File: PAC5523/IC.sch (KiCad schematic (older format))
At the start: 17 parts

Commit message: updated schematic
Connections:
- net 3V3 is gone; now on net +5V: U?.8 (VCC)
- net VIO is gone; now on net +5V: U?.16 (VCC), U?.5 (VBUS), U?.5 (VBUS), U?.5 (VBUS)
- net VSYS is gone; now on net +5V: U?.3 (VDD)
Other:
- moved on the sheet: C?, D?, L?, R?, U?

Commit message: updated schematic
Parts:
- C?: value 10uF -> 100n; footprint Capacitor_SMD:C_0805_2012Metric -> Capacitor_SMD:C_0603_1608Metric
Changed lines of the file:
@@
 P 2550 1300
 F 0 "C?" H 2642 1346 50  0000 L CNN
-F 1 "10uF" H 2642 1255 50  0000 L CNN
-F 2 "Capacitor_SMD:C_0805_2012Metric" H 2550 1300 50  0001 C CNN
+F 1 "100n" H 2642 1255 50  0000 L CNN
+F 2 "Capacitor_SMD:C_0603_1608Metric" H 2550 1300 50  0001 C CNN
 F 3 "~" H 2550 1300 50  0001 C CNN
 	1    2550 1300

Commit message: wip
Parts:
- U4: renamed from U?; footprint Package_SO:SOIC-16W_5.3x10.2mm_P1.27mm -> Package_SO:SOIC-16_3.9x9.9mm_P1.27mm
- U5: renamed from U?; footprint (none) -> Package_TO_SOT_SMD:SOT-23-5
- gave numbers to parts that had none: 15
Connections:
- net ENC_B: no longer U3.4 (RXD)
- net RS485RXTX: no longer U3.1 (TXD)
- new net CANRX: U3.4 (RXD)
- new net CANTX: U3.1 (TXD)

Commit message: wip
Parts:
- D17: footprint Diode_SMD:D_SMA -> Diode_SMD:D_SOD-123F
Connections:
- net Ain: now also U9.6 (IO4); no longer U7.6 (IO4)
- net CANRX: now also U6.1 (DI), U9.1 (IO1)
- net CANTX: now also U6.4 (DO), U9.3 (IO2)
- net HALL1: now also U8.4 (IO3); no longer U8.6 (IO4)
- net HALL2: now also U8.6 (IO4); no longer U8.4 (IO3)
- net NTC: now also U7.1 (IO1); no longer U7.4 (IO3)
- net SWDCL: now also U7.6 (IO4); no longer U9.6 (IO4)
- net SWDIO: now also U7.4 (IO3); no longer U9.4 (IO3)
- removed net UART_RX: U6.4 (DO), U9.1 (IO1)
- removed net UART_TX: U6.1 (DI), U9.3 (IO2)
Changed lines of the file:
@@
 F 0 "D17" H 2550 2005 50  0000 C CNN
 F 1 "SS310" H 2550 1914 50  0000 C CNN
-F 2 "Diode_SMD:D_SMA" V 2550 1800 50  0001 C CNN
+F 2 "Diode_SMD:D_SOD-123F" V 2550 1800 50  0001 C CNN
 F 3 "~" V 2550 1800 50  0001 C CNN
 	1    2550 1800
@@
 Wire Wire Line
 	6200 4550 6200 4650
-Text GLabel 6200 4750 0    50   Input ~ 0
-UART_RX
-Text GLabel 6200 4450 0    50   Input ~ 0
-UART_TX
 $Comp
 L otter:RS485 U6
@@
 	1    0    0    -1
 $EndComp
+Text GLabel 9550 3350 2    50   Input ~ 0
+SWDCL
+Text GLabel 9550 3450 2    50   Input ~ 0
+SWDIO
+Text GLabel 8950 3250 0    50   Input ~ 0
+NTC
 Text GLabel 9550 4550 2    50   Input ~ 0
-SWDCL
-Text GLabel 9550 4650 2    50   Input ~ 0
-SWDIO
-Text GLabel 9550 3450 2    50   Input ~ 0
-NTC
-Text GLabel 9550 3350 2    50   Input ~ 0
 Ain
 $Comp
@@
 	1    0    0    -1
 $EndComp
-Text GLabel 8950 4450 0    50   Input ~ 0
-UART_RX
-Text GLabel 8950 4550 0    50   Input ~ 0
-UART_TX
 $Comp
 L power:GND #PWR0166
@@
 Text GLabel 8950 3850 0    50   Input ~ 0
 HALL3
+Text GLabel 9550 3950 2    50   Input ~ 0
+HALL2
 Text GLabel 9550 4050 2    50   Input ~ 0
-HALL2
-Text GLabel 9550 3950 2    50   Input ~ 0
 HALL1
 $Comp
@@
 Text GLabel 2350 3600 0    50   Input ~ 0
 CANTX
+Text GLabel 8950 4450 0    50   Input ~ 0
+CANRX
+Text GLabel 8950 4550 0    50   Input ~ 0
+CANTX
+Text GLabel 6200 4750 0    50   Input ~ 0
+CANTX
+Text GLabel 6200 4450 0    50   Input ~ 0
+CANRX
 $EndSCHEMATC

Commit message: wip
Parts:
- U5: footprint Package_TO_SOT_SMD:SOT-23-5 -> Package_TO_SOT_SMD:SOT-353_SC-70-5
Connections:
- net NTC: now also U7.4 (IO3); no longer U7.1 (IO1)
- net SWDCL: now also U7.3 (IO2); no longer U7.6 (IO4)
- net SWDIO: now also U7.1 (IO1); no longer U7.4 (IO3)
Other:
- note removed: "Braucht Footprint ^"
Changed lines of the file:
@@
 	1    0    0    -1
 $EndComp
-Text Notes 5950 3700 0    50   ~ 0
-Braucht Footprint ^
 Text GLabel 6850 3300 2    50   Input ~ 0
 SK6812_OUT
@@
 F 0 "U5" H 6525 3525 50  0000 C CNN
 F 1 "NL17SZ125" H 6525 3434 50  0000 C CNN
-F 2 "Package_TO_SOT_SMD:SOT-23-5" H 6500 3400 50  0001 C CNN
+F 2 "Package_TO_SOT_SMD:SOT-353_SC-70-5" H 6500 3400 50  0001 C CNN
 F 3 "https://lcsc.com/product-detail/Logic-ICs_ON-Semicon_NL17SZ125DFT2G_ON-Semicon-ON-NL17SZ125DFT2G_C97774.html" H 6500 3400 50  0001 C CNN
 	1    6500 3200
@@
 	1    0    0    -1
 $EndComp
-Text GLabel 9550 3350 2    50   Input ~ 0
+Text GLabel 8950 3350 0    50   Input ~ 0
 SWDCL
+Text GLabel 8950 3250 0    50   Input ~ 0
+SWDIO
 Text GLabel 9550 3450 2    50   Input ~ 0
-SWDIO
-Text GLabel 8950 3250 0    50   Input ~ 0
 NTC
 Text GLabel 9550 4550 2    50   Input ~ 0

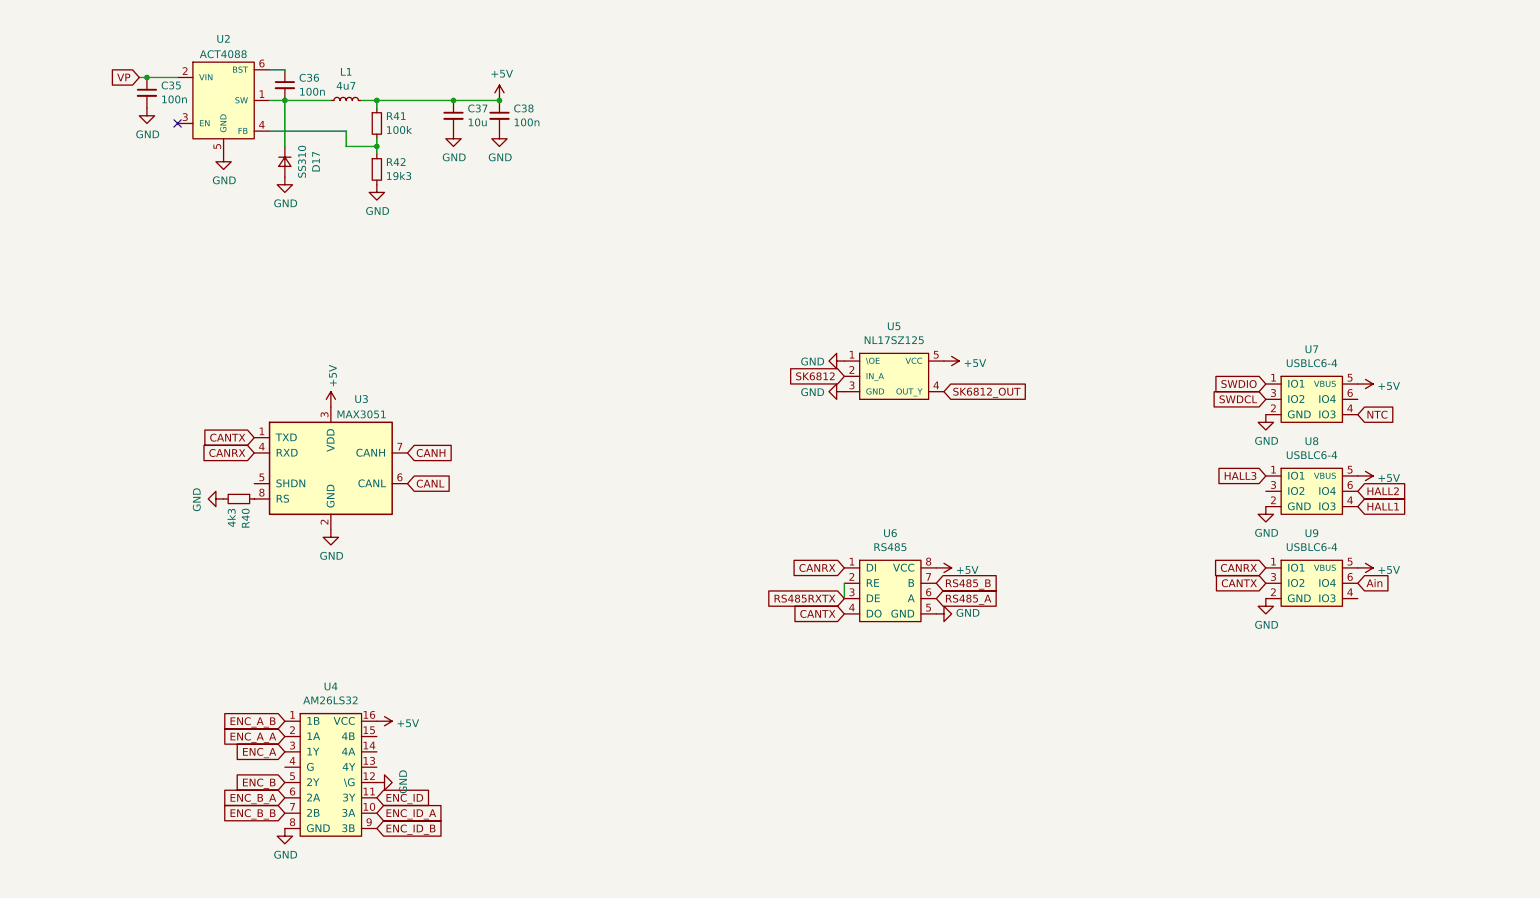
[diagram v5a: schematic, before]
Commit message: added Encoder,LED,NTC
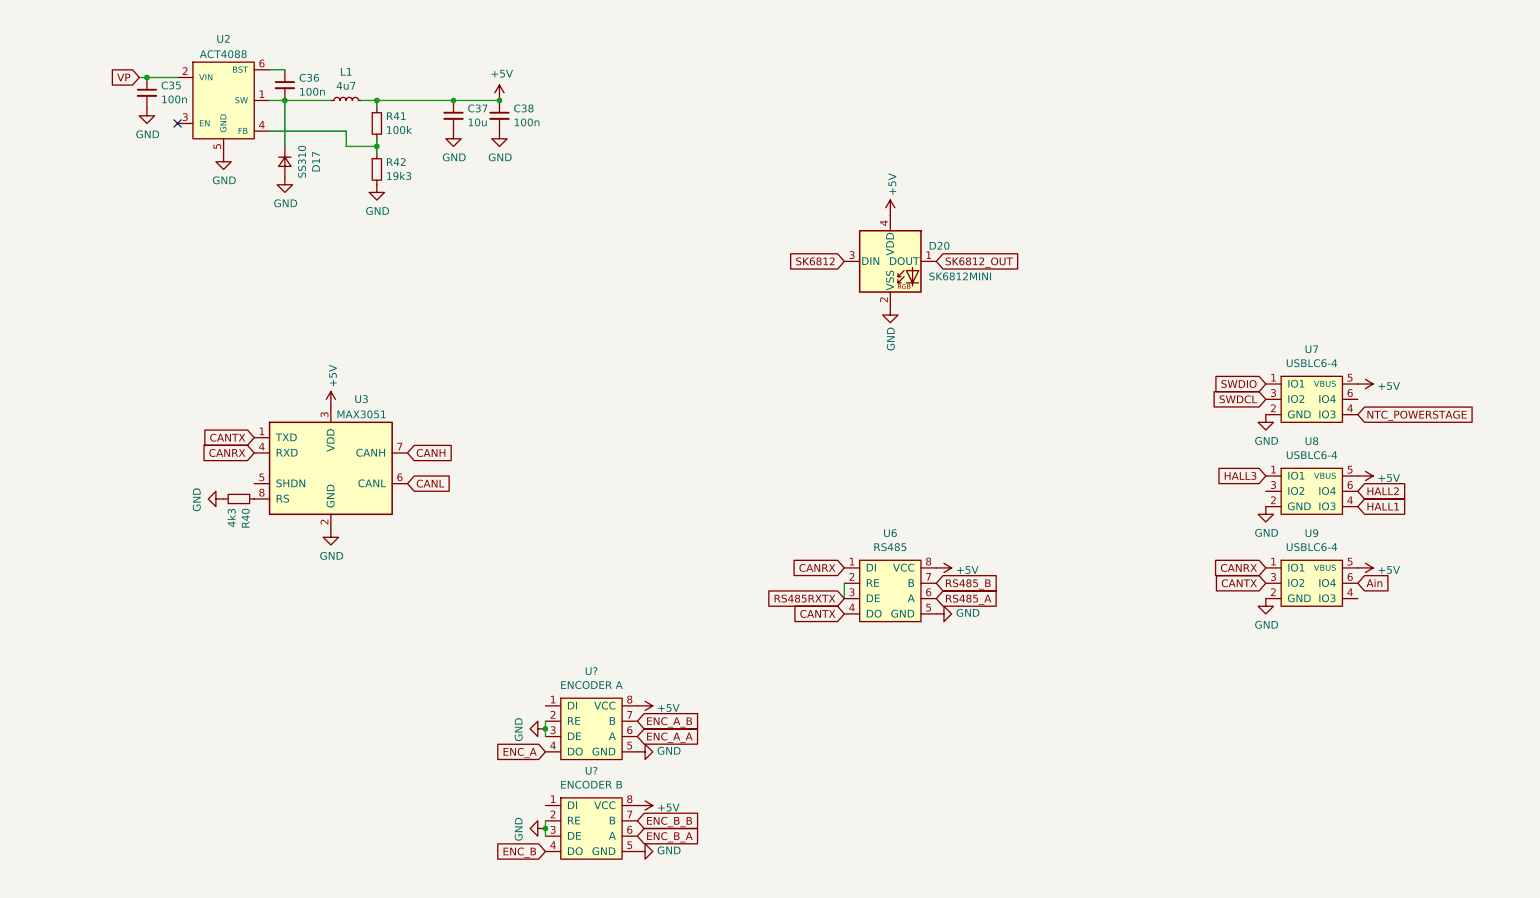
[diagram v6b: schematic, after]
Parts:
- removed U4: AM26LS32, Package_SO:SOIC-16_3.9x9.9mm_P1.27mm, symbol otter:AM26LS32
- removed U5: NL17SZ125, Package_TO_SOT_SMD:SOT-353_SC-70-5, symbol otter:NL17SZ125
- added D20: SK6812MINI, LED_SMD:LED_SK6812MINI_PLCC4_3.5x3.5mm_P1.75mm, symbol LED:SK6812MINI
- added U?: ENCODER A, Package_SO:SOIC-8_3.9x4.9mm_P1.27mm, symbol otter:RS485
- added U?: ENCODER B, Package_SO:SOIC-8_3.9x4.9mm_P1.27mm, symbol otter:RS485
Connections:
- net +5V: now also D20.4 (VDD), U?.8 (VCC), U?.8 (VCC)
- net ENC_A: now also U?.4 (DO)
- net ENC_A_A: now also U?.6 (A)
- net ENC_A_B: now also U?.7 (B)
- net ENC_B: now also U?.4 (DO)
- net ENC_B_A: now also U?.6 (A)
- net ENC_B_B: now also U?.7 (B)
- net GND: now also D20.2 (VSS), U?.2 (RE), U?.2 (RE), U?.3 (DE), U?.3 (DE), U?.5 (GND), U?.5 (GND)
- net SK6812: now also D20.3 (DIN)
- net SK6812_OUT: now also D20.1 (DOUT)
- net NTC renamed NTC_POWERSTAGE
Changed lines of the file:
@@
 L power:+5V #PWR0150
 U 1 1 5D5D3803
-P 6850 3100
-F 0 "#PWR0150" H 6850 2950 50  0001 C CNN
-F 1 "+5V" V 6865 3228 50  0000 L CNN
-F 2 "" H 6850 3100 50  0001 C CNN
-F 3 "" H 6850 3100 50  0001 C CNN
-	1    6850 3100
-	0    1    1    0
+P 6500 2150
+F 0 "#PWR0150" H 6500 2000 50  0001 C CNN
+F 1 "+5V" V 6515 2278 50  0000 L CNN
+F 2 "" H 6500 2150 50  0001 C CNN
+F 3 "" H 6500 2150 50  0001 C CNN
+	1    6500 2150
+	1    0    0    -1
 $EndComp
 Connection ~ 3950 1400
@@
 	1    0    0    -1
 $EndComp
-Text GLabel 6850 3300 2    50   Input ~ 0
+Text GLabel 6800 2450 2    50   Input ~ 0
 SK6812_OUT
-Text GLabel 6200 3200 0    50   Input ~ 0
+Text GLabel 6200 2450 0    50   Input ~ 0
 SK6812
-$Comp
-L power:GND #PWR0158
-U 1 1 5D5D3883
-P 6200 3100
-F 0 "#PWR0158" H 6200 2850 50  0001 C CNN
-F 1 "GND" V 6205 2972 50  0000 R CNN
-F 2 "" H 6200 3100 50  0001 C CNN
-F 3 "" H 6200 3100 50  0001 C CNN
-	1    6200 3100
-	0    1    1    0
-$EndComp
 $Comp
 L power:GND #PWR0159
 U 1 1 5D5D3889
-P 6200 3300
-F 0 "#PWR0159" H 6200 3050 50  0001 C CNN
-F 1 "GND" V 6205 3172 50  0000 R CNN
-F 2 "" H 6200 3300 50  0001 C CNN
-F 3 "" H 6200 3300 50  0001 C CNN
-	1    6200 3300
-	0    1    1    0
-$EndComp
-$Comp
-L otter:NL17SZ125 U5
-U 1 1 5D5D388F
-P 6500 3200
-F 0 "U5" H 6525 3525 50  0000 C CNN
-F 1 "NL17SZ125" H 6525 3434 50  0000 C CNN
-F 2 "Package_TO_SOT_SMD:SOT-353_SC-70-5" H 6500 3400 50  0001 C CNN
-F 3 "https://lcsc.com/product-detail/Logic-ICs_ON-Semicon_NL17SZ125DFT2G_ON-Semicon-ON-NL17SZ125DFT2G_C97774.html" H 6500 3400 50  0001 C CNN
-	1    6500 3200
+P 6500 2750
+F 0 "#PWR0159" H 6500 2500 50  0001 C CNN
+F 1 "GND" V 6505 2622 50  0000 R CNN
+F 2 "" H 6500 2750 50  0001 C CNN
+F 3 "" H 6500 2750 50  0001 C CNN
+	1    6500 2750
 	1    0    0    -1
 $EndComp
@@
 	1    0    0    -1
 $EndComp
-$Comp
-L power:GND #PWR0162
-U 1 1 5D5D38C4
-P 3150 5850
-F 0 "#PWR0162" H 3150 5600 50  0001 C CNN
-F 1 "GND" H 3155 5677 50  0000 C CNN
-F 2 "" H 3150 5850 50  0001 C CNN
-F 3 "" H 3150 5850 50  0001 C CNN
-	1    3150 5850
-	0    -1   -1   0
-$EndComp
-Text GLabel 3150 6150 2    50   Input ~ 0
-ENC_ID_B
-Text GLabel 3150 6050 2    50   Input ~ 0
-ENC_ID_A
-Text GLabel 2550 6050 0    50   Input ~ 0
+Text GLabel 4850 6100 2    50   Input ~ 0
 ENC_B_B
-Text GLabel 2550 5950 0    50   Input ~ 0
+Text GLabel 4850 6200 2    50   Input ~ 0
 ENC_B_A
-Text GLabel 2550 5550 0    50   Input ~ 0
+Text GLabel 4850 5550 2    50   Input ~ 0
 ENC_A_A
-Text GLabel 2550 5450 0    50   Input ~ 0
+Text GLabel 4850 5450 2    50   Input ~ 0
 ENC_A_B
-$Comp
-L power:GND #PWR0163
-U 1 1 5D5D38D1
-P 2550 6150
-F 0 "#PWR0163" H 2550 5900 50  0001 C CNN
-F 1 "GND" H 2555 5977 50  0000 C CNN
-F 2 "" H 2550 6150 50  0001 C CNN
-F 3 "" H 2550 6150 50  0001 C CNN
-	1    2550 6150
-	1    0    0    -1
-$EndComp
-$Comp
-L otter:AM26LS32 U4
-U 1 1 5D5D38D7
-P 2850 5800
-F 0 "U4" H 2850 6375 50  0000 C CNN
-F 1 "AM26LS32" H 2850 6284 50  0000 C CNN
-F 2 "Package_SO:SOIC-16_3.9x9.9mm_P1.27mm" H 2850 6350 50  0001 C CNN
-F 3 "https://lcsc.com/product-detail/Driver-ICs_TI_AM26C32IDR_AM26C32IDR_C36693.html" H 2850 6350 50  0001 C CNN
-	1    2850 5800
-	1    0    0    -1
-$EndComp
-Text GLabel 2550 5850 0    50   Input ~ 0
+Text GLabel 4250 6300 0    50   Input ~ 0
 ENC_B
-Text GLabel 2550 5650 0    50   Input ~ 0
+Text GLabel 4250 5650 0    50   Input ~ 0
 ENC_A
-Text GLabel 3150 5950 2    50   Input ~ 0
-ENC_ID
 $Comp
 L power:GND #PWR0164
@@
 SWDIO
 Text GLabel 9550 3450 2    50   Input ~ 0
-NTC
+NTC_POWERSTAGE
 Text GLabel 9550 4550 2    50   Input ~ 0
 Ain
@@
 Text GLabel 9550 4050 2    50   Input ~ 0
 HALL1
-$Comp
-L power:+5V #PWR0168
-U 1 1 5D6006D6
-P 3150 5450
-F 0 "#PWR0168" H 3150 5300 50  0001 C CNN
-F 1 "+5V" V 3165 5578 50  0000 L CNN
-F 2 "" H 3150 5450 50  0001 C CNN
-F 3 "" H 3150 5450 50  0001 C CNN
-	1    3150 5450
-	0    1    1    0
-$EndComp
 $Comp
 L power:+5V #PWR0169
@@
 Text GLabel 6200 4450 0    50   Input ~ 0
 CANRX
+$Comp
+L LED:SK6812MINI D20
+U 1 1 5CDB4E22
+P 6500 2450
+F 0 "D20" H 6750 2550 50  0000 L CNN
+F 1 "SK6812MINI" H 6750 2350 50  0000 L CNN
+F 2 "LED_SMD:LED_SK6812MINI_PLCC4_3.5x3.5mm_P1.75mm" H 6550 2150 50  0001 L TNN
+F 3 "https://cdn-shop.adafruit.com/product-files/2686/SK6812MINI_REV.01-1-2.pdf" H 6600 2075 50  0001 L TNN
+	1    6500 2450
+	1    0    0    -1
+$EndComp
+$Comp
+L power:GND #PWR?
+U 1 1 5CDFFD7B
+P 4850 5650
+F 0 "#PWR?" H 4850 5400 50  0001 C CNN
+F 1 "GND" V 4855 5522 50  0000 R CNN
+F 2 "" H 4850 5650 50  0001 C CNN
+F 3 "" H 4850 5650 50  0001 C CNN
+	1    4850 5650
+	0    -1   -1   0
+$EndComp
+Wire Wire Line
+	4250 5450 4250 5500
+$Comp
+L otter:RS485 U?
+U 1 1 5CDFFD85
+P 4550 5500
+F 0 "U?" H 4550 5875 50  0000 C CNN
+F 1 "ENCODER A" H 4550 5784 50  0000 C CNN
+F 2 "Package_SO:SOIC-8_3.9x4.9mm_P1.27mm" H 4550 5750 50  0001 C CNN
+F 3 "" H 4550 5750 50  0001 C CNN
+	1    4550 5500
+	1    0    0    -1
+$EndComp
+$Comp
+L power:+5V #PWR?
+U 1 1 5CDFFD8B
+P 4850 5350
+F 0 "#PWR?" H 4850 5200 50  0001 C CNN
+F 1 "+5V" V 4865 5478 50  0000 L CNN
+F 2 "" H 4850 5350 50  0001 C CNN
+F 3 "" H 4850 5350 50  0001 C CNN
+	1    4850 5350
+	0    1    1    0
+$EndComp
+$Comp
+L power:GND #PWR?
+U 1 1 5CE00508
+P 4850 6300
+F 0 "#PWR?" H 4850 6050 50  0001 C CNN
+F 1 "GND" V 4855 6172 50  0000 R CNN
+F 2 "" H 4850 6300 50  0001 C CNN
+F 3 "" H 4850 6300 50  0001 C CNN
+	1    4850 6300
+	0    -1   -1   0
+$EndComp
+Wire Wire Line
+	4250 6100 4250 6150
+$Comp
+L otter:RS485 U?
+U 1 1 5CE00512
+P 4550 6150
+F 0 "U?" H 4550 6525 50  0000 C CNN
+F 1 "ENCODER B" H 4550 6434 50  0000 C CNN
+F 2 "Package_SO:SOIC-8_3.9x4.9mm_P1.27mm" H 4550 6400 50  0001 C CNN
+F 3 "" H 4550 6400 50  0001 C CNN
+	1    4550 6150
+	1    0    0    -1
+$EndComp
+$Comp
+L power:+5V #PWR?
+U 1 1 5CE00518
+P 4850 6000
+F 0 "#PWR?" H 4850 5850 50  0001 C CNN
+F 1 "+5V" V 4865 6128 50  0000 L CNN
+F 2 "" H 4850 6000 50  0001 C CNN
+F 3 "" H 4850 6000 50  0001 C CNN
+	1    4850 6000
+	0    1    1    0
+$EndComp
+$Comp
+L power:GND #PWR?
+U 1 1 5CE03BAB
+P 4250 6150
+F 0 "#PWR?" H 4250 5900 50  0001 C CNN
+F 1 "GND" H 4255 5977 50  0000 C CNN
+F 2 "" H 4250 6150 50  0001 C CNN
+F 3 "" H 4250 6150 50  0001 C CNN
+	1    4250 6150
+	0    1    1    0
+$EndComp
+$Comp
+L power:GND #PWR?
+U 1 1 5CE03EB0
+P 4250 5500
+F 0 "#PWR?" H 4250 5250 50  0001 C CNN
+F 1 "GND" H 4255 5327 50  0000 C CNN
+F 2 "" H 4250 5500 50  0001 C CNN
+F 3 "" H 4250 5500 50  0001 C CNN
+	1    4250 5500
+	0    1    1    0
+$EndComp
+Connection ~ 4250 5500
+Wire Wire Line
+	4250 5500 4250 5550
+Connection ~ 4250 6150
+Wire Wire Line
+	4250 6150 4250 6200
 $EndSCHEMATC

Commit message: wip
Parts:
- gave numbers to parts that had none: 2
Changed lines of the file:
@@
 $EndComp
 $Comp
-L power:GND #PWR?
+L power:GND #PWR0168
 U 1 1 5CDFFD7B
 P 4850 5650
-F 0 "#PWR?" H 4850 5400 50  0001 C CNN
+F 0 "#PWR0168" H 4850 5400 50  0001 C CNN
 F 1 "GND" V 4855 5522 50  0000 R CNN
 F 2 "" H 4850 5650 50  0001 C CNN
@@
 	4250 5450 4250 5500
 $Comp
-L otter:RS485 U?
+L otter:RS485 U5
 U 1 1 5CDFFD85
 P 4550 5500
-F 0 "U?" H 4550 5875 50  0000 C CNN
+F 0 "U5" H 4550 5875 50  0000 C CNN
 F 1 "ENCODER A" H 4550 5784 50  0000 C CNN
 F 2 "Package_SO:SOIC-8_3.9x4.9mm_P1.27mm" H 4550 5750 50  0001 C CNN
@@
 $EndComp
 $Comp
-L power:+5V #PWR?
+L power:+5V #PWR0182
 U 1 1 5CDFFD8B
 P 4850 5350
-F 0 "#PWR?" H 4850 5200 50  0001 C CNN
+F 0 "#PWR0182" H 4850 5200 50  0001 C CNN
 F 1 "+5V" V 4865 5478 50  0000 L CNN
 F 2 "" H 4850 5350 50  0001 C CNN
@@
 $EndComp
 $Comp
-L power:GND #PWR?
+L power:GND #PWR0183
 U 1 1 5CE00508
 P 4850 6300
-F 0 "#PWR?" H 4850 6050 50  0001 C CNN
+F 0 "#PWR0183" H 4850 6050 50  0001 C CNN
 F 1 "GND" V 4855 6172 50  0000 R CNN
 F 2 "" H 4850 6300 50  0001 C CNN
@@
 	4250 6100 4250 6150
 $Comp
-L otter:RS485 U?
+L otter:RS485 U11
 U 1 1 5CE00512
 P 4550 6150
-F 0 "U?" H 4550 6525 50  0000 C CNN
+F 0 "U11" H 4550 6525 50  0000 C CNN
 F 1 "ENCODER B" H 4550 6434 50  0000 C CNN
 F 2 "Package_SO:SOIC-8_3.9x4.9mm_P1.27mm" H 4550 6400 50  0001 C CNN
@@
 $EndComp
 $Comp
-L power:+5V #PWR?
+L power:+5V #PWR0184
 U 1 1 5CE00518
 P 4850 6000
-F 0 "#PWR?" H 4850 5850 50  0001 C CNN
+F 0 "#PWR0184" H 4850 5850 50  0001 C CNN
 F 1 "+5V" V 4865 6128 50  0000 L CNN
 F 2 "" H 4850 6000 50  0001 C CNN
@@
 $EndComp
 $Comp
-L power:GND #PWR?
+L power:GND #PWR0185
 U 1 1 5CE03BAB
 P 4250 6150
-F 0 "#PWR?" H 4250 5900 50  0001 C CNN
+F 0 "#PWR0185" H 4250 5900 50  0001 C CNN
 F 1 "GND" H 4255 5977 50  0000 C CNN
 F 2 "" H 4250 6150 50  0001 C CNN
@@
 $EndComp
 $Comp
-L power:GND #PWR?
+L power:GND #PWR0186
 U 1 1 5CE03EB0
 P 4250 5500
-F 0 "#PWR?" H 4250 5250 50  0001 C CNN
+F 0 "#PWR0186" H 4250 5250 50  0001 C CNN
 F 1 "GND" H 4255 5327 50  0000 C CNN
 F 2 "" H 4250 5500 50  0001 C CNN

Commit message: placement almost done
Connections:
- net NTC_POWERSTAGE: now also U7.6 (IO4); no longer U7.4 (IO3)
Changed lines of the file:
@@
 Text GLabel 8950 3250 0    50   Input ~ 0
 SWDIO
-Text GLabel 9550 3450 2    50   Input ~ 0
+Text GLabel 9550 3350 2    50   Input ~ 0
 NTC_POWERSTAGE
 Text GLabel 9550 4550 2    50   Input ~ 0
